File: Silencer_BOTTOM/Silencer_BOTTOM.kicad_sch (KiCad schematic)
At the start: 45 parts, among them IC1 TL072, IC2 AS3360, IC3 TL072, IC4 AS3360

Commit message: Add PWR_FLAG to nets
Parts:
- removed POWER1: Synth_power_2x5, AO_tht:Power_Header, symbol AO_symbols:Synth_power_2x5
- added J1: Conn_02x05_Odd_Even, symbol Connector_Generic:Conn_02x05_Odd_Even
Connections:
- net +12V_1: no longer C1.1, C15.1, C16.1, C8.1, FERRITE1.1, IC1.8 (V+), IC3.8 (V+)
- net -12V_1: no longer C17.2, C18.2, C2.2, C9.2, FERRITE2.1, IC1.4 (V-), IC3.4 (V-)
- net GND_1: now also J1.3 (Pin_3), J1.4 (Pin_4), J1.5 (Pin_5), J1.6 (Pin_6), J1.7 (Pin_7), J1.8 (Pin_8)
- net at D2.1 (K): now also J1.1 (Pin_1), J1.2 (Pin_2)
- net at D1.2 (A): now also J1.10 (Pin_10), J1.9 (Pin_9)
- new net +12V: C1.1, C15.1, C16.1, C8.1, FERRITE1.1, IC1.8 (V+), IC3.8 (V+)
- new net -12V: C17.2, C18.2, C2.2, C9.2, FERRITE2.1, IC1.4 (V-), IC3.4 (V-)

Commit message: Panel layout and artwork (near?) complete.
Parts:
- C1, C10, C13, C14, C16, C18, C2, C3, C6, C7, C8, C9: footprint (none) -> Capacitor_THT:C_Disc_D3.0mm_W2.0mm_P2.50mm
- C11, C12, C15, C17, C4, C5: footprint (none) -> Capacitor_THT:CP_Radial_D6.3mm_P2.50mm
- FERRITE1, FERRITE2, R1, R10, R11, R12, R13, R14, R15, R16, R2, R3, R4, R5, R6, R7, R8, R9: footprint (none) -> Resistor_THT:R_Axial_DIN0207_L6.3mm_D2.5mm_P10.16mm_Horizontal
- IC2, IC4: footprint (none) -> Package_DIP:DIP-14_W7.62mm_LongPads
- J1: footprint (none) -> AO_tht:Power_Header
- JP1, JP2: footprint (none) -> Connector_PinHeader_2.54mm:PinHeader_1x08_P2.54mm_Vertical
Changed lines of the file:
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@@
 			)
 		)
-		(property "Footprint" ""
+		(property "Footprint" "Capacitor_THT:C_Disc_D3.0mm_W2.0mm_P2.50mm"
 			(at 83.5152 52.07 0)
 			(effects
@@
 			)
 		)
-		(property "Footprint" ""
+		(property "Footprint" "Resistor_THT:R_Axial_DIN0207_L6.3mm_D2.5mm_P10.16mm_Horizontal"
 			(at 143.51 127.508 90)
 			(effects
@@
 			)
 		)
-		(property "Footprint" ""
+		(property "Footprint" "Resistor_THT:R_Axial_DIN0207_L6.3mm_D2.5mm_P10.16mm_Horizontal"
 			(at 40.132 148.59 90)
 			(effects
@@
 			)
 		)
-		(property "Footprint" ""
+		(property "Footprint" "Resistor_THT:R_Axial_DIN0207_L6.3mm_D2.5mm_P10.16mm_Horizontal"
 			(at 137.668 129.54 90)
 			(effects
@@
 			)
 		)
-		(property "Footprint" ""
+		(property "Footprint" "Resistor_THT:R_Axial_DIN0207_L6.3mm_D2.5mm_P10.16mm_Horizontal"
 			(at 31.242 118.11 90)
 			(effects
@@
 			)
 		)
-		(property "Footprint" ""
+		(property "Footprint" "Capacitor_THT:C_Disc_D3.0mm_W2.0mm_P2.50mm"
 			(at 83.5152 39.37 0)
 			(effects
@@
 			)
 		)
-		(property "Footprint" ""
+		(property "Footprint" "Resistor_THT:R_Axial_DIN0207_L6.3mm_D2.5mm_P10.16mm_Horizontal"
 			(at 155.702 101.6 90)
 			(effects
@@
 			)
 		)
-		(property "Footprint" ""
+		(property "Footprint" "Capacitor_THT:C_Disc_D3.0mm_W2.0mm_P2.50mm"
 			(at 97.79 140.0048 0)
 			(effects
@@
 			)
 		)
-		(property "Footprint" ""
+		(property "Footprint" "Resistor_THT:R_Axial_DIN0207_L6.3mm_D2.5mm_P10.16mm_Horizontal"
 			(at 267.97 110.998 90)
 			(effects
@@
 			)
 		)
-		(property "Footprint" ""
+		(property "Footprint" "Capacitor_THT:C_Disc_D3.0mm_W2.0mm_P2.50mm"
 			(at 97.4852 39.37 0)
 			(effects
@@
 			)
 		)
-		(property "Footprint" ""
+		(property "Footprint" "Capacitor_THT:C_Disc_D3.0mm_W2.0mm_P2.50mm"
 			(at 222.25 123.4948 0)
 			(effects
@@
 			)
 		)
-		(property "Footprint" ""
+		(property "Footprint" "Capacitor_THT:C_Disc_D3.0mm_W2.0mm_P2.50mm"
 			(at 97.4852 52.07 0)
 			(effects
@@
 			)
 		)
-		(property "Footprint" ""
+		(property "Footprint" "Capacitor_THT:C_Disc_D3.0mm_W2.0mm_P2.50mm"
 			(at 205.74 123.4948 0)
 			(effects
@@
 			)
 		)
-		(property "Footprint" ""
+		(property "Footprint" "Capacitor_THT:CP_Radial_D6.3mm_P2.50mm"
 			(at 54.3052 52.07 0)
 			(effects
@@
 			)
 		)
-		(property "Footprint" ""
+		(property "Footprint" "Resistor_THT:R_Axial_DIN0207_L6.3mm_D2.5mm_P10.16mm_Horizontal"
 			(at 25.4 116.078 90)
 			(effects
@@
 			)
 		)
-		(property "Footprint" ""
+		(property "Footprint" "Connector_PinHeader_2.54mm:PinHeader_1x08_P2.54mm_Vertical"
 			(at 265.43 40.64 0)
 			(effects
@@
 			)
 		)
-		(property "Footprint" ""
+		(property "Footprint" "Resistor_THT:R_Axial_DIN0207_L6.3mm_D2.5mm_P10.16mm_Horizontal"
 			(at 231.902 90.17 90)
 			(effects
@@
 			)
 		)
-		(property "Footprint" ""
+		(property "Footprint" "AO_tht:Power_Header"
 			(at 172.72 41.91 0)
 			(effects
@@
 			)
 		)
-		(property "Footprint" ""
+		(property "Footprint" "Resistor_THT:R_Axial_DIN0207_L6.3mm_D2.5mm_P10.16mm_Horizontal"
 			(at 164.592 132.08 90)
 			(effects
@@
 			)
 		)
-		(property "Footprint" ""
+		(property "Footprint" "Capacitor_THT:C_Disc_D3.0mm_W2.0mm_P2.50mm"
 			(at 68.2752 39.37 0)
 			(effects
@@
 			)
 		)
-		(property "Footprint" ""
+		(property "Footprint" "Capacitor_THT:CP_Radial_D6.3mm_P2.50mm"
 			(at 44.1452 121.92 0)
 			(effects
@@
 			)
 		)
-		(property "Footprint" ""
+		(property "Footprint" "Capacitor_THT:CP_Radial_D6.3mm_P2.50mm"
 			(at 124.7648 133.35 0)
 			(effects
@@
 			)
 		)
-		(property "Footprint" ""
+		(property "Footprint" "Connector_PinHeader_2.54mm:PinHeader_1x08_P2.54mm_Vertical"
 			(at 236.22 40.64 0)
 			(effects
@@
 			)
 		)
-		(property "Footprint" ""
+		(property "Footprint" "Resistor_THT:R_Axial_DIN0207_L6.3mm_D2.5mm_P10.16mm_Horizontal"
 			(at 196.85 113.538 90)
 			(effects
@@
 			)
 		)
-		(property "Footprint" ""
+		(property "Footprint" "Resistor_THT:R_Axial_DIN0207_L6.3mm_D2.5mm_P10.16mm_Horizontal"
 			(at 107.442 106.68 90)
 			(effects
@@
 			)
 		)
-		(property "Footprint" ""
+		(property "Footprint" "Capacitor_THT:C_Disc_D3.0mm_W2.0mm_P2.50mm"
 			(at 81.28 140.0048 0)
 			(effects
@@
 			)
 		)
-		(property "Footprint" ""
+		(property "Footprint" "Package_DIP:DIP-14_W7.62mm_LongPads"
 			(at 229.87 124.46 0)
 			(effects
@@
 			)
 		)
-		(property "Footprint" ""
+		(property "Footprint" "Package_DIP:DIP-14_W7.62mm_LongPads"
 			(at 105.41 140.97 0)
 			(effects
@@
 			)
 		)
-		(property "Footprint" ""
+		(property "Footprint" "Capacitor_THT:C_Disc_D3.0mm_W2.0mm_P2.50mm"
 			(at 215.9 93.0148 0)
 			(effects
@@
 			)
 		)
-		(property "Footprint" ""
+		(property "Footprint" "Capacitor_THT:CP_Radial_D6.3mm_P2.50mm"
 			(at 168.6052 105.41 0)
 			(effects
@@
 			)
 		)
-		(property "Footprint" ""
+		(property "Footprint" "Capacitor_THT:CP_Radial_D6.3mm_P2.50mm"
 			(at 54.3052 39.37 0)
 			(effects
@@
 			)
 		)
-		(property "Footprint" ""
+		(property "Footprint" "Capacitor_THT:C_Disc_D3.0mm_W2.0mm_P2.50mm"
 			(at 91.44 109.5248 0)
 			(effects
@@
 			)
 		)
-		(property "Footprint" ""
+		(property "Footprint" "Resistor_THT:R_Axial_DIN0207_L6.3mm_D2.5mm_P10.16mm_Horizontal"
 			(at 262.128 113.03 90)
 			(effects
@@
 			)
 		)
-		(property "Footprint" ""
+		(property "Footprint" "Resistor_THT:R_Axial_DIN0207_L6.3mm_D2.5mm_P10.16mm_Horizontal"
 			(at 149.86 99.568 90)
 			(effects
@@
 			)
 		)
-		(property "Footprint" ""
+		(property "Footprint" "Resistor_THT:R_Axial_DIN0207_L6.3mm_D2.5mm_P10.16mm_Horizontal"
 			(at 135.89 33.528 90)
 			(effects
@@
 			)
 		)
-		(property "Footprint" ""
+		(property "Footprint" "Resistor_THT:R_Axial_DIN0207_L6.3mm_D2.5mm_P10.16mm_Horizontal"
 			(at 233.68 119.888 90)
 			(effects
@@
 			)
 		)
-		(property "Footprint" ""
+		(property "Footprint" "Resistor_THT:R_Axial_DIN0207_L6.3mm_D2.5mm_P10.16mm_Horizontal"
 			(at 72.39 130.048 90)
 			(effects
@@
 			)
 		)
-		(property "Footprint" ""
+		(property "Footprint" "Resistor_THT:R_Axial_DIN0207_L6.3mm_D2.5mm_P10.16mm_Horizontal"
 			(at 135.89 53.848 90)
 			(effects
@@
 			)
 		)
-		(property "Footprint" ""
+		(property "Footprint" "Capacitor_THT:CP_Radial_D6.3mm_P2.50mm"
 			(at 249.2248 116.84 0)
 			(effects
@@
 			)
 		)
-		(property "Footprint" ""
+		(property "Footprint" "Capacitor_THT:C_Disc_D3.0mm_W2.0mm_P2.50mm"
 			(at 68.2752 52.07 0)
 			(effects
@@
 			)
 		)
-		(property "Footprint" ""
+		(property "Footprint" "Resistor_THT:R_Axial_DIN0207_L6.3mm_D2.5mm_P10.16mm_Horizontal"
 			(at 109.22 136.398 90)
 			(effects

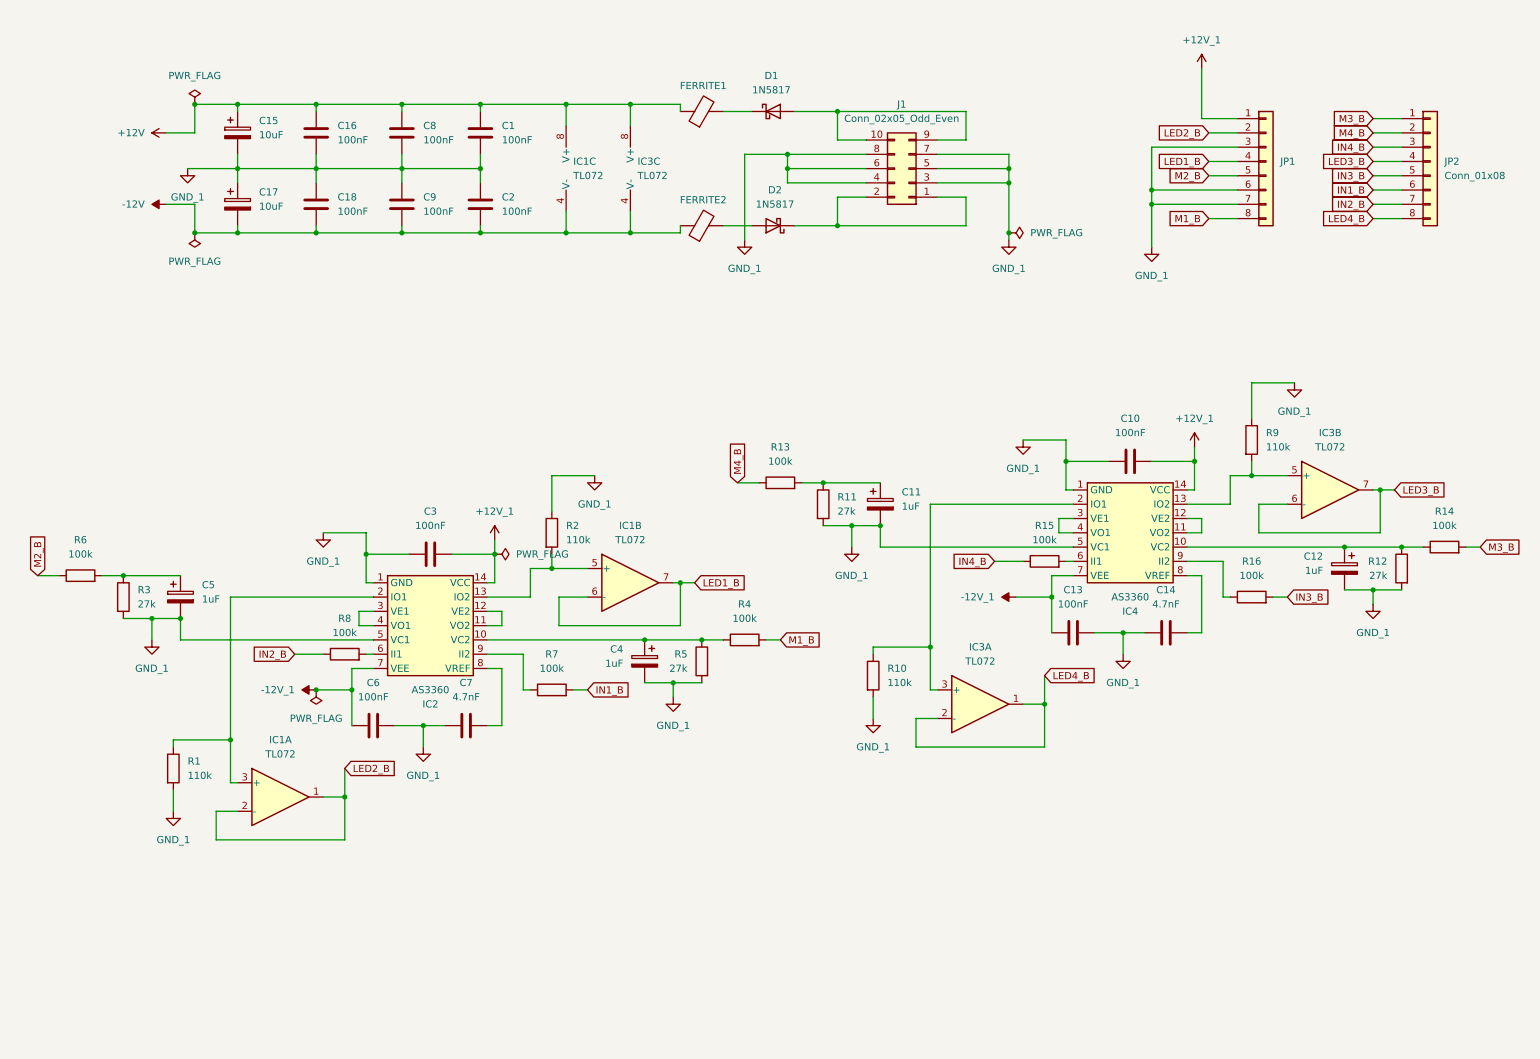
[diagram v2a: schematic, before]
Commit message: Refactor Top and Bottom Schematics.
Had to move input/output jacks to bottom board.  This required a full refactoring of both and will mean re-doing the pcb layout of the top board.
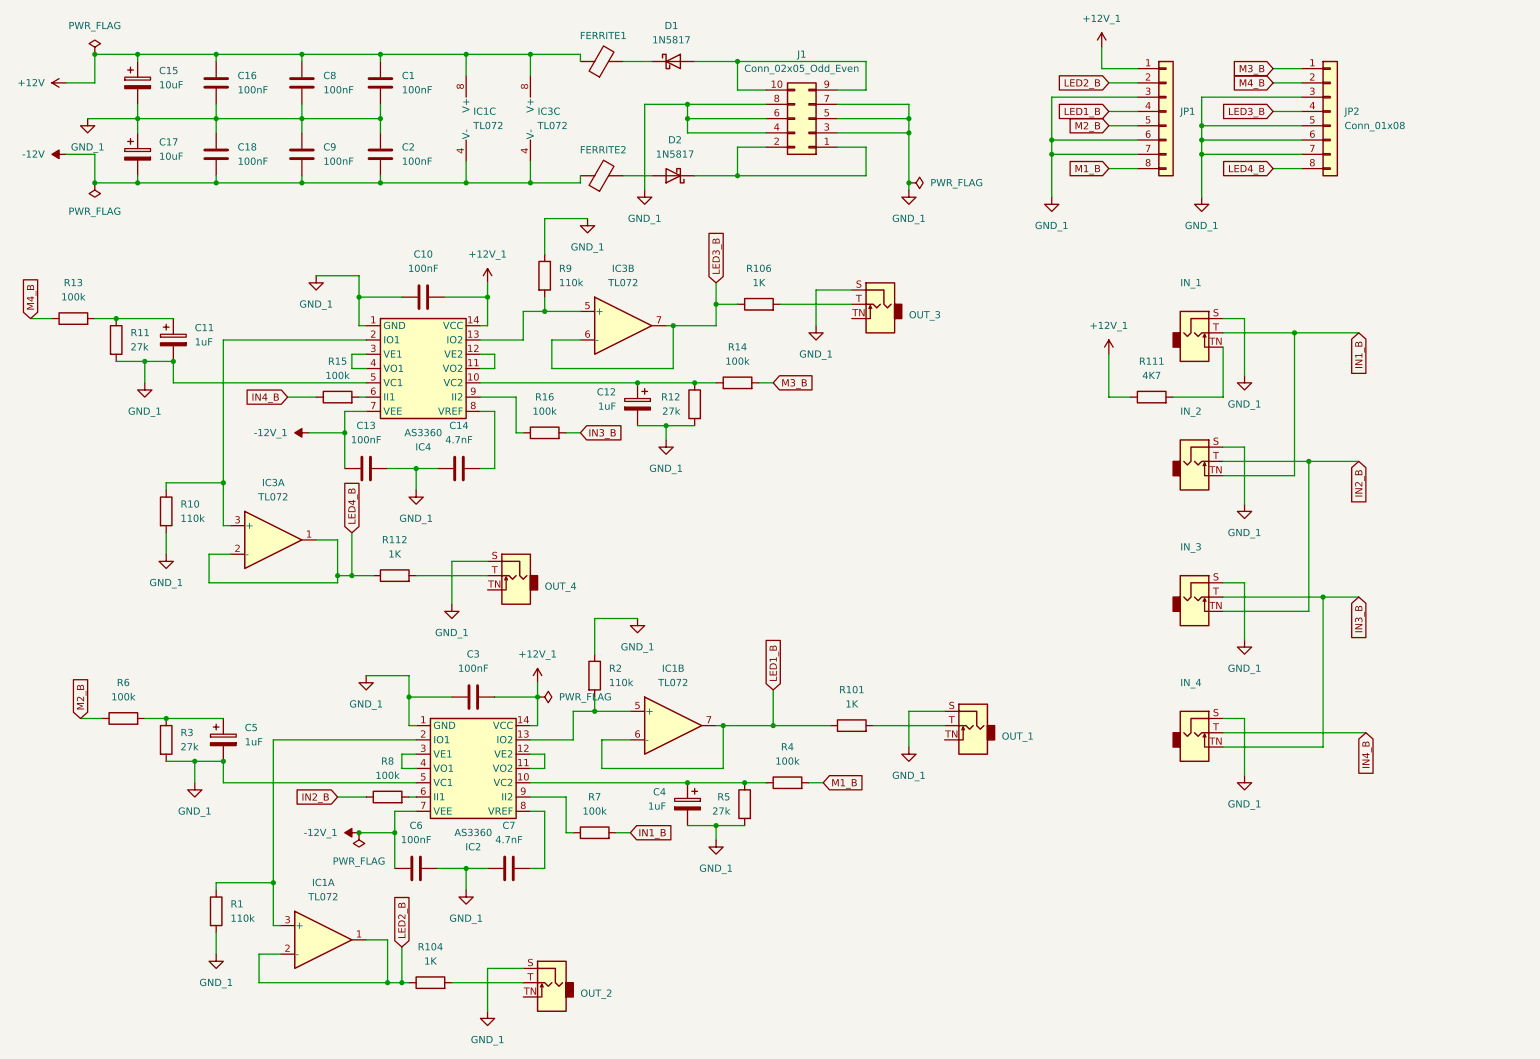
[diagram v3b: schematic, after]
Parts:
- added IN_1, IN_2, IN_3, IN_4, OUT_1, OUT_2, OUT_3, OUT_4: AudioJack2_SwitchT, AO_tht:Jack_6.35mm_PJ_629HAN_slots, symbol AO_symbols:AudioJack2_SwitchT
- added R101, R104, R106, R112: 1K, AO_tht:R_Axial_DIN0207_L6.3mm_D2.5mm_P10.16mm_Horizontal, symbol Device:R
- added R111: 4K7, AO_tht:R_Axial_DIN0207_L6.3mm_D2.5mm_P10.16mm_Horizontal, symbol Device:R
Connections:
- net +12V_1: now also R111.1
- net GND_1: now also JP2.3 (Pin_3), JP2.5 (Pin_5), JP2.6 (Pin_6), JP2.7 (Pin_7), IN_1.S, IN_2.S, IN_3.S, IN_4.S, OUT_1.S, OUT_2.S, OUT_3.S, OUT_4.S
- net IN1_B: now also IN_1.T, IN_2.TN; no longer JP2.6 (Pin_6)
- net IN2_B: now also IN_2.T, IN_3.TN; no longer JP2.7 (Pin_7)
- net IN3_B: now also IN_3.T, IN_4.TN; no longer JP2.5 (Pin_5)
- net IN4_B: now also IN_4.T; no longer JP2.3 (Pin_3)
- net LED1_B: now also R101.1
- net LED2_B: now also R104.1
- net LED3_B: now also R106.1
- net LED4_B: now also R112.1
- new net: OUT_2.T, R104.2
- new net: IN_1.TN, R111.2
- new net: OUT_4.T, R112.2
- new net: OUT_3.T, R106.2
- new net: OUT_1.T, R101.2
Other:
- moved on the sheet: C1, C10, C11, C12, C13, C14, C15, C16, C17, C18, C2, C3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
